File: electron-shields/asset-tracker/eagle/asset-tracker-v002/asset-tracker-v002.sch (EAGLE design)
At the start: 25 parts, among them J1 1X2-3.5MM, T1 DMG3415, U1 FGPMMOPA6H, U3 LIS3DHTR, X1 ELECTRON, X2 uFL, X7 SMA-SMD

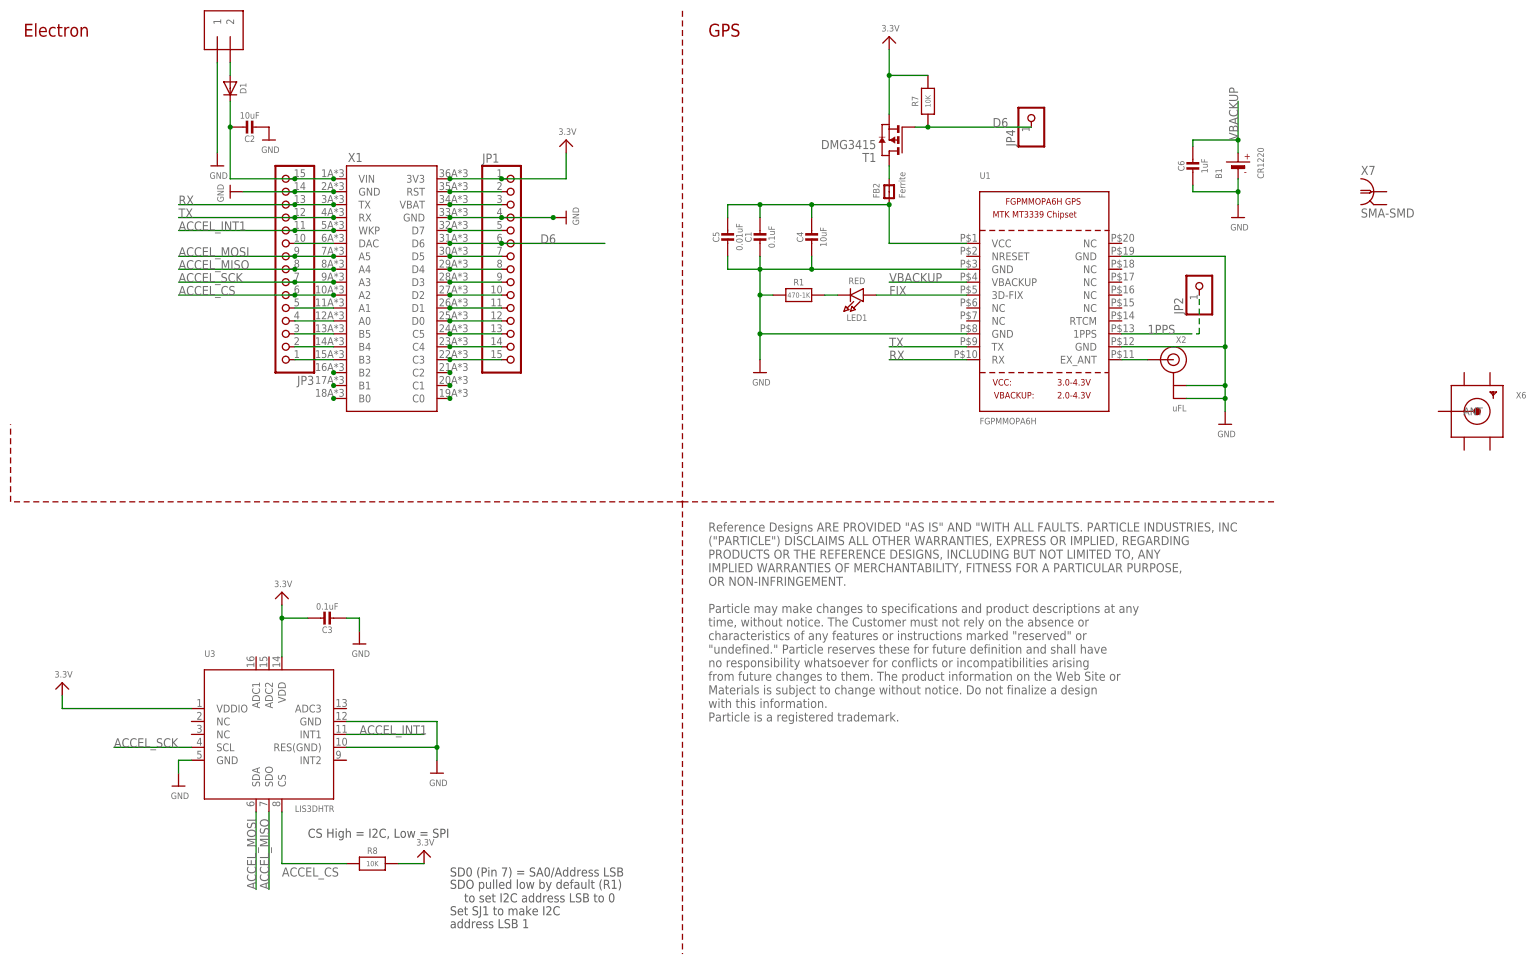
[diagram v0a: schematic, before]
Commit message: replaced uff with SMA and changed GPS module location
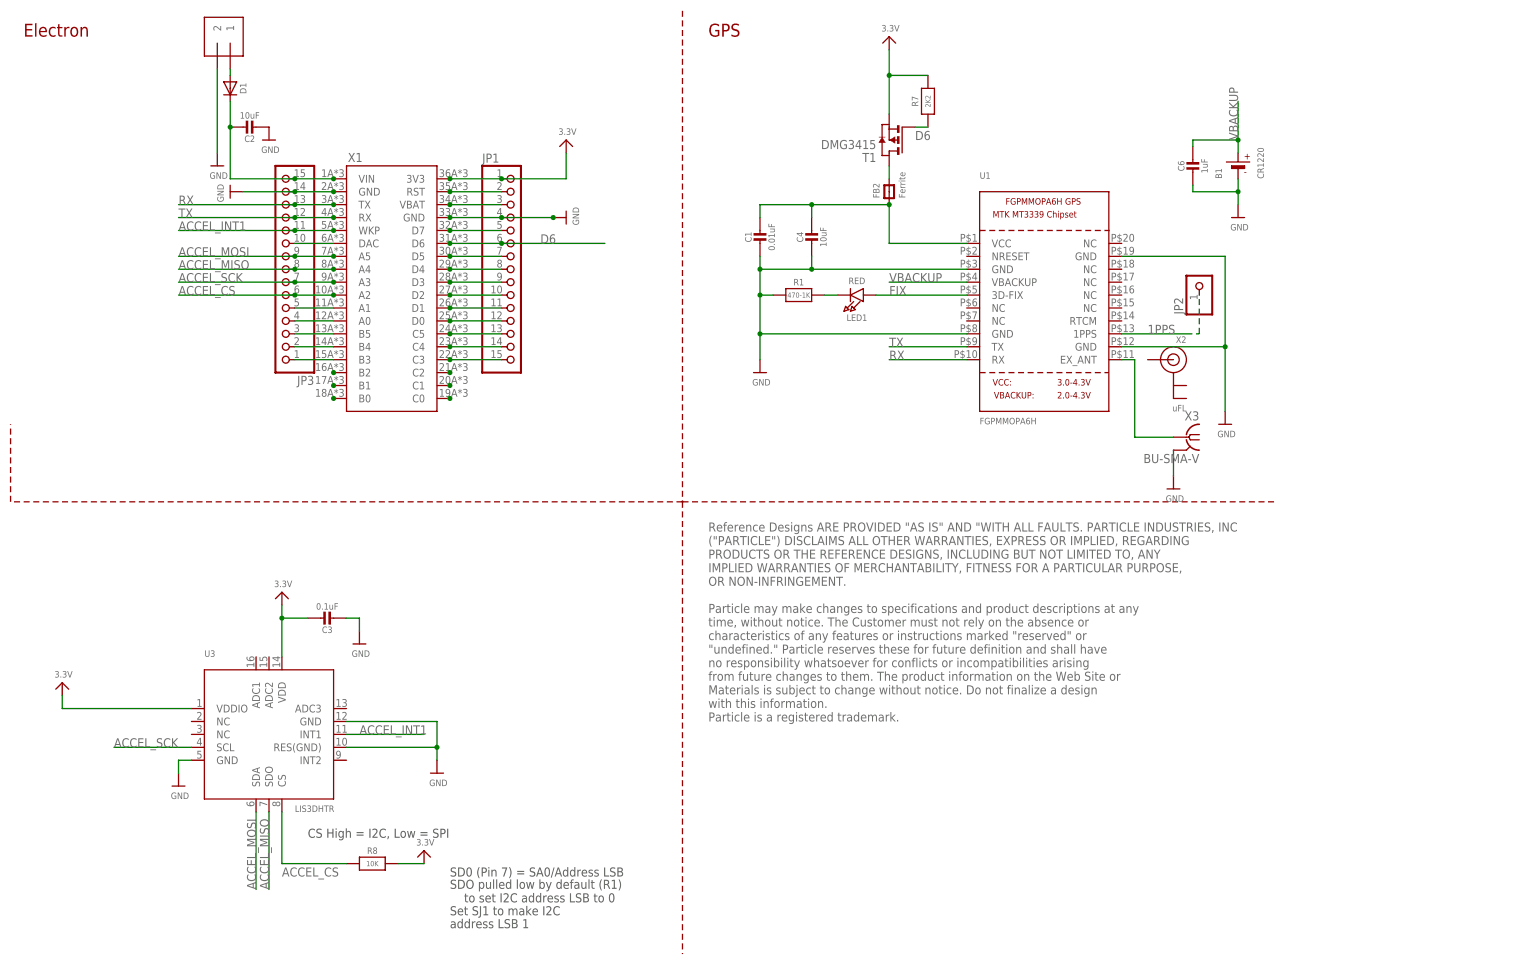
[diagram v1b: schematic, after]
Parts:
- removed C5: 0.01uF, microbuilder:CAP_CERAMIC0805-NOOUTLINE
- removed JP4: (no value), microbuilder:HEADER-1X1ROUND
- removed X6: (no value), adafruit:SMACONNECTOR_EDGE_UFL
- removed X7: SMA-SMD, con-coax:SMA-SMD
- added X3: BU-SMA-V, con-coax:BU-SMA-V
- C1: value 0.1uF -> 0.01uF
- R7: value 10K -> 2K2
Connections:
- net D6: no longer JP4.1
- net GND: now also J1.2, X3.2; no longer C5.2, J1.1, X2.GND@0, X2.GND@1
- net N$1: no longer C5.1
- net N$4: now also X3.1; no longer X2.SIGNAL
- net N$9: now also J1.1; no longer J1.2
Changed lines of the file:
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@@
 <part name="R1" library="microbuilder" deviceset="RESISTOR" device="0805_NOOUTLINE" value="470-1K"/>
 <part name="U$2" library="microbuilder" deviceset="GND" device=""/>
-<part name="C1" library="microbuilder" deviceset="CAP_CERAMIC" device="0805-NOOUTLINE" value="0.1uF"/>
+<part name="C1" library="microbuilder" deviceset="CAP_CERAMIC" device="0805-NOOUTLINE" value="0.01uF"/>
 <part name="B1" library="microbuilder" deviceset="BATTERY" device="CR1220_SMT" value="CR1220"/>
 <part name="U$14" library="microbuilder" deviceset="GND" device=""/>
@@
 <part name="JP3" library="microbuilder" deviceset="HEADER-1X15" device=""/>
 <part name="T1" library="zetex" deviceset="PMOSSOT23" device="" value="DMG3415"/>
-<part name="R7" library="microbuilder" deviceset="RESISTOR" device="0805_NOOUTLINE" value="10K"/>
+<part name="R7" library="microbuilder" deviceset="RESISTOR" device="0805_NOOUTLINE" value="2K2"/>
 <part name="U$15" library="microbuilder" deviceset="3.3V" device=""/>
-<part name="JP4" library="microbuilder" deviceset="HEADER-1X1" device="ROUND"/>
-<part name="C5" library="microbuilder" deviceset="CAP_CERAMIC" device="0805-NOOUTLINE" value="0.01uF"/>
 <part name="C6" library="microbuilder" deviceset="CAP_CERAMIC" device="0805-NOOUTLINE" value="1uF"/>
-<part name="X6" library="adafruit" deviceset="SMACONNECTOR" device="_EDGE_UFL"/>
-<part name="X7" library="con-coax" deviceset="SMA-SMD" device=""/>
+<part name="X3" library="con-coax" deviceset="BU-SMA-V" device=""/>
+<part name="U$4" library="microbuilder" deviceset="GND" device=""/>
 </parts>
 <sheets>
@@
 <instance part="C2" gate="G$1" x="48.26" y="162.56" rot="R90"/>
 <instance part="U$5" gate="G$1" x="50.8" y="160.02"/>
-<instance part="J1" gate="G$1" x="43.18" y="180.34" rot="R90"/>
+<instance part="J1" gate="G$1" x="40.64" y="179.07" rot="MR90"/>
 <instance part="U$1" gate="G$1" x="109.22" y="144.78" rot="R90"/>
 <instance part="D1" gate="G$1" x="43.18" y="170.18" rot="R270"/>
@@
 <instance part="R7" gate="G$1" x="180.34" y="167.64" rot="R90"/>
 <instance part="U$15" gate="G$1" x="172.72" y="180.34"/>
-<instance part="JP4" gate="G$1" x="200.66" y="165.1" rot="R90"/>
-<instance part="C5" gate="G$1" x="140.97" y="139.7"/>
 <instance part="C6" gate="G$1" x="232.41" y="153.67"/>
-<instance part="X6" gate="G$1" x="288.29" y="106.68"/>
-<instance part="X7" gate="G$1" x="267.97" y="149.86"/>
+<instance part="X3" gate="G$1" x="231.14" y="101.6" rot="MR0"/>
+<instance part="U$4" gate="G$1" x="228.6" y="91.44"/>
 </instances>
 <busses>
@@
 <wire x1="157.48" y1="137.16" x2="157.48" y2="134.62" width="0.1524" layer="91"/>
 <junction x="157.48" y="134.62"/>
-<pinref part="C5" gate="G$1" pin="2"/>
-<wire x1="140.97" y1="137.16" x2="140.97" y2="134.62" width="0.1524" layer="91"/>
-<wire x1="140.97" y1="134.62" x2="147.32" y2="134.62" width="0.1524" layer="91"/>
 </segment>
 <segment>
 <wire x1="218.44" y1="119.38" x2="238.76" y2="119.38" width="0.1524" layer="91"/>
-<wire x1="238.76" y1="119.38" x2="238.76" y2="111.76" width="0.1524" layer="91"/>
-<wire x1="238.76" y1="111.76" x2="238.76" y2="109.22" width="0.1524" layer="91"/>
-<wire x1="238.76" y1="109.22" x2="238.76" y2="106.68" width="0.1524" layer="91"/>
+<wire x1="238.76" y1="119.38" x2="238.76" y2="106.68" width="0.1524" layer="91"/>
 <wire x1="218.44" y1="137.16" x2="238.76" y2="137.16" width="0.1524" layer="91"/>
 <wire x1="238.76" y1="137.16" x2="238.76" y2="119.38" width="0.1524" layer="91"/>
-<wire x1="231.14" y1="109.22" x2="238.76" y2="109.22" width="0.1524" layer="91"/>
-<wire x1="231.14" y1="111.76" x2="238.76" y2="111.76" width="0.1524" layer="91"/>
 <junction x="238.76" y="119.38"/>
-<junction x="238.76" y="109.22"/>
-<junction x="238.76" y="111.76"/>
 <pinref part="U1" gate="G$1" pin="GND@3"/>
 <pinref part="U$19" gate="G$1" pin="GND"/>
 <pinref part="U1" gate="G$1" pin="GND@4"/>
-<pinref part="X2" gate="G$1" pin="GND@1"/>
-<pinref part="X2" gate="G$1" pin="GND@0"/>
 </segment>
 <segment>
@@
 </segment>
 <segment>
-<pinref part="U$3" gate="G$1" pin="GND"/>
-<wire x1="40.64" y1="175.26" x2="40.64" y2="157.48" width="0.1524" layer="91"/>
-<pinref part="J1" gate="G$1" pin="1"/>
-</segment>
-<segment>
 <pinref part="C2" gate="G$1" pin="2"/>
 <pinref part="U$5" gate="G$1" pin="GND"/>
@@
 <pinref part="JP1" gate="G$1" pin="4"/>
 </segment>
+<segment>
+<pinref part="X3" gate="G$1" pin="2"/>
+<wire x1="228.6" y1="99.06" x2="228.6" y2="93.98" width="0.1524" layer="91"/>
+<pinref part="U$4" gate="G$1" pin="GND"/>
+</segment>
+<segment>
+<pinref part="U$3" gate="G$1" pin="GND"/>
+<pinref part="J1" gate="G$1" pin="2"/>
+<wire x1="40.64" y1="157.48" x2="40.64" y2="173.99" width="0.1524" layer="91"/>
+</segment>
 </net>
 <net name="3.3V" class="0">
@@
 <junction x="55.88" y="147.32"/>
 <pinref part="JP3" gate="G$1" pin="13"/>
-</segment>
-</net>
-<net name="N$4" class="0">
-<segment>
-<wire x1="218.44" y1="116.84" x2="223.52" y2="116.84" width="0.1524" layer="91"/>
-<pinref part="U1" gate="G$1" pin="EX_ANT"/>
-<pinref part="X2" gate="G$1" pin="SIGNAL"/>
 </segment>
 </net>
@@
 <wire x1="157.48" y1="147.32" x2="157.48" y2="144.78" width="0.1524" layer="91"/>
 <junction x="157.48" y="147.32"/>
-<pinref part="C5" gate="G$1" pin="1"/>
-<wire x1="140.97" y1="144.78" x2="140.97" y2="147.32" width="0.1524" layer="91"/>
-<wire x1="140.97" y1="147.32" x2="147.32" y2="147.32" width="0.1524" layer="91"/>
-<junction x="147.32" y="147.32"/>
 </segment>
 </net>
@@
 <segment>
 <wire x1="180.34" y1="162.56" x2="177.8" y2="162.56" width="0.1524" layer="91"/>
-<junction x="180.34" y="162.56"/>
 <pinref part="R7" gate="G$1" pin="1"/>
 <pinref part="T1" gate="A" pin="G"/>
-<wire x1="180.34" y1="162.56" x2="200.66" y2="162.56" width="0.1524" layer="91"/>
-<label x="193.04" y="162.56" size="1.778" layer="95"/>
-<pinref part="JP4" gate="G$1" pin="1"/>
+<label x="177.8" y="160.02" size="1.778" layer="95"/>
 </segment>
 </net>
@@
 </segment>
 </net>
-<net name="N$9" class="0">
-<segment>
-<pinref part="D1" gate="G$1" pin="A"/>
-<pinref part="J1" gate="G$1" pin="2"/>
-<wire x1="43.18" y1="172.72" x2="43.18" y2="175.26" width="0.1524" layer="91"/>
-</segment>
-</net>
 <net name="VCC" class="0">
 <segment>
@@
 </segment>
 </net>
+<net name="N$4" class="0">
+<segment>
+<pinref part="U1" gate="G$1" pin="EX_ANT"/>
+<wire x1="218.44" y1="116.84" x2="220.98" y2="116.84" width="0.1524" layer="91"/>
+<wire x1="220.98" y1="116.84" x2="220.98" y2="101.6" width="0.1524" layer="91"/>
+<pinref part="X3" gate="G$1" pin="1"/>
+<wire x1="220.98" y1="101.6" x2="228.6" y2="101.6" width="0.1524" layer="91"/>
+</segment>
+</net>
+<net name="N$9" class="0">
+<segment>
+<pinref part="D1" gate="G$1" pin="A"/>
+<pinref part="J1" gate="G$1" pin="1"/>
+<wire x1="43.18" y1="173.99" x2="43.18" y2="172.72" width="0.1524" layer="91"/>
+</segment>
+</net>
